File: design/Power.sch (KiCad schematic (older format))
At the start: 50 parts, among them U2 NCP1117ST33T3G, U3 DRV8302

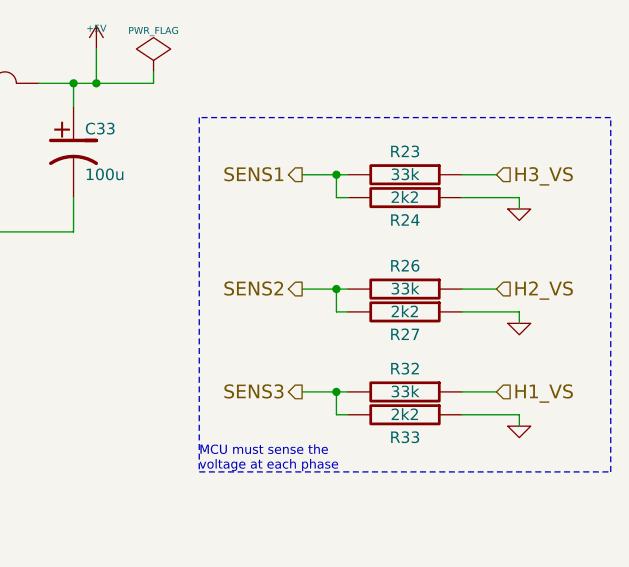
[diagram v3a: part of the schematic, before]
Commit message: Changed voltage divider resistor to 39k
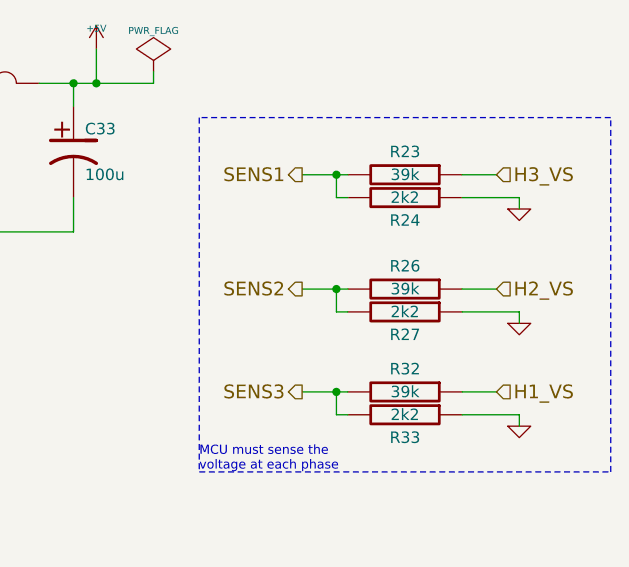
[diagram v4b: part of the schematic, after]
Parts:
- R23, R26, R32: value 33k -> 39k
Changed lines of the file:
@@
 LIBS:crf_1
 LIBS:BLDC_4-cache
-EELAYER 25 0
+EELAYER 24 0
 EELAYER END
 $Descr A4 11693 8268
@@
 P 10200 3350
 F 0 "R23" V 10100 3350 50  0000 C CNN
-F 1 "33k" V 10200 3350 50  0000 C CNN
+F 1 "39k" V 10200 3350 50  0000 C CNN
 F 2 "SMD_Packages:SMD-0603_r" H 10200 3350 60  0001 C CNN
 F 3 "" H 10200 3350 60  0001 C CNN
@@
 P 10200 3850
 F 0 "R26" V 10100 3850 50  0000 C CNN
-F 1 "33k" V 10200 3850 50  0000 C CNN
+F 1 "39k" V 10200 3850 50  0000 C CNN
 F 2 "SMD_Packages:SMD-0603_r" H 10200 3850 60  0001 C CNN
 F 3 "" H 10200 3850 60  0001 C CNN
@@
 P 10200 4300
 F 0 "R32" V 10100 4300 50  0000 C CNN
-F 1 "33k" V 10200 4300 50  0000 C CNN
+F 1 "39k" V 10200 4300 50  0000 C CNN
 F 2 "SMD_Packages:SMD-0603_r" H 10200 4300 60  0001 C CNN
 F 3 "" H 10200 4300 60  0001 C CNN
@@
 00 FD 87 A8 17 00 00 00 00 F4 1F A2 5E 00 00 00 00 D0 7F 88 7A 01 00 00 00 40 FF 21 EA 05 00 00
 00 00 FD 87 A8 17 00 00 00 00 F4 1F A2 5E 00 00 00 00 D0 7F 88 7A 01 00 00 00 40 FF 21 EA 05 00
-00 00 00 FD F7 3F 90 37 91 24 49 74 FD E2 00 00 00 00 49 45 4E 44 AE 42 60 82 00
+00 00 00 FD F7 3F 90 37 91 24 49 74 FD E2 00 00 00 00 49 45 4E 44 AE 42 60 82 2E
 EndData
 $EndBitmap
@@
 0D 0D 85 50 5B 08 A1 71 E3 C6 45 47 47 77 AB F8 CD C0 F0 65 C3 18 9A 0F 4F 4B 4B 4B 51 51 51 53
 53 93 40 20 30 31 31 61 94 40 19 18 18 43 C3 C0 C0 A0 72 FE 07 CF 64 8C 61 E1 12 74 DD 00 00 00
-00 49 45 4E 44 AE 42 60 82 05
+00 49 45 4E 44 AE 42 60 82 6A
 EndData
 $EndBitmap
@@
 20 10 88 31 C3 77 F3 62 81 40 20 10 08 04 02 81 E0 1F 14 E4 21 10 08 04 02 81 40 8C 41 50 90 87
 40 20 10 08 04 02 31 06 41 41 1E 02 81 40 20 10 08 C4 18 E4 FF 01 14 B1 03 90 4A B9 68 69 00 00
-00 00 49 45 4E 44 AE 42 60 82 00
+00 00 49 45 4E 44 AE 42 60 82 2D
 EndData
 $EndBitmap
@@
 A1 C7 18 00 00 C0 28 C8 B2 00 00 00 46 41 96 05 00 00 30 0A B2 2C 00 00 80 51 90 65 01 00 00 8C
 82 2C 0B 00 00 60 14 64 59 00 00 00 A3 FC 7F BD 9B 69 A6 C1 67 F0 EA 00 00 00 00 49 45 4E 44 AE
-42 60 82 00
+42 60 82 6B
 EndData
 $EndBitmap
@@
 AB D8 39 0B 59 91 9E DF A8 2A 5B EE 54 3A FD 71 ED 71 2F 29 C3 82 EC 80 87 06 6E C3 98 10 30 3B
 62 9A BB 2D 03 B8 C4 64 FC B5 26 AC 13 9B D1 39 40 41 C1 D6 78 4C 84 BF 94 F0 6F E1 BF 96 F0 0F
-FF 77 E2 FF 1F 0F 43 55 32 21 1C 08 16 00 00 00 00 49 45 4E 44 AE 42 60 82 27
+FF 77 E2 FF 1F 0F 43 55 32 21 1C 08 16 00 00 00 00 49 45 4E 44 AE 42 60 82 60
 EndData
 $EndBitmap

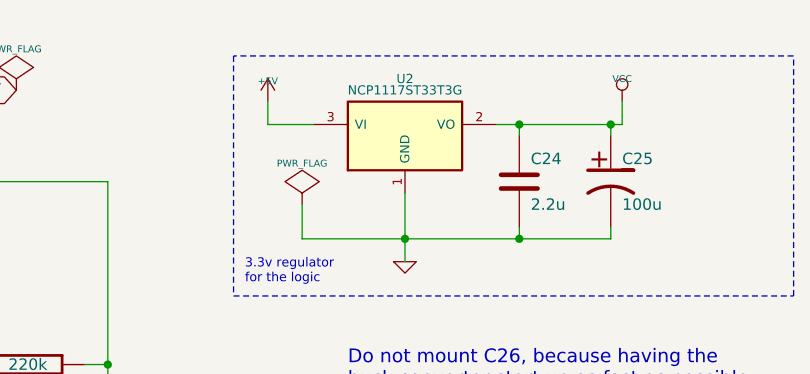
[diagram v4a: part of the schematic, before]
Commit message: Changed FETs and VREG part number to make things a bit more clear
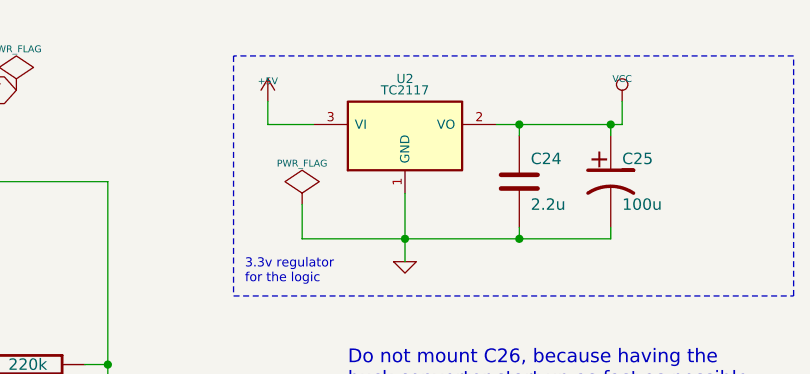
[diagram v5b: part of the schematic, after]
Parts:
- U2: value NCP1117ST33T3G -> TC2117
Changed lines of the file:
@@
 P 6300 1200
 F 0 "U2" H 6300 1450 40  0000 C CNN
-F 1 "NCP1117ST33T3G" H 6300 1400 40  0000 C CNN
+F 1 "TC2117" H 6300 1400 40  0000 C CNN
 F 2 "SMD_Packages:SOT-223" H 6300 1200 60  0001 C CNN
 F 3 "" H 6300 1200 60  0000 C CNN
@@
 00 FD 87 A8 17 00 00 00 00 F4 1F A2 5E 00 00 00 00 D0 7F 88 7A 01 00 00 00 40 FF 21 EA 05 00 00
 00 00 FD 87 A8 17 00 00 00 00 F4 1F A2 5E 00 00 00 00 D0 7F 88 7A 01 00 00 00 40 FF 21 EA 05 00
-00 00 00 FD F7 3F 90 37 91 24 49 74 FD E2 00 00 00 00 49 45 4E 44 AE 42 60 82 2E
+00 00 00 FD F7 3F 90 37 91 24 49 74 FD E2 00 00 00 00 49 45 4E 44 AE 42 60 82 4D
 EndData
 $EndBitmap
@@
 0D 0D 85 50 5B 08 A1 71 E3 C6 45 47 47 77 AB F8 CD C0 F0 65 C3 18 9A 0F 4F 4B 4B 4B 51 51 51 53
 53 93 40 20 30 31 31 61 94 40 19 18 18 43 C3 C0 C0 A0 72 FE 07 CF 64 8C 61 E1 12 74 DD 00 00 00
-00 49 45 4E 44 AE 42 60 82 6A
+00 49 45 4E 44 AE 42 60 82 32
 EndData
 $EndBitmap
@@
 20 10 88 31 C3 77 F3 62 81 40 20 10 08 04 02 81 E0 1F 14 E4 21 10 08 04 02 81 40 8C 41 50 90 87
 40 20 10 08 04 02 31 06 41 41 1E 02 81 40 20 10 08 C4 18 E4 FF 01 14 B1 03 90 4A B9 68 69 00 00
-00 00 49 45 4E 44 AE 42 60 82 2D
+00 00 49 45 4E 44 AE 42 60 82 4C
 EndData
 $EndBitmap
@@
 A1 C7 18 00 00 C0 28 C8 B2 00 00 00 46 41 96 05 00 00 30 0A B2 2C 00 00 80 51 90 65 01 00 00 8C
 82 2C 0B 00 00 60 14 64 59 00 00 00 A3 FC 7F BD 9B 69 A6 C1 67 F0 EA 00 00 00 00 49 45 4E 44 AE
-42 60 82 6B
+42 60 82 D7
 EndData
 $EndBitmap
@@
 AB D8 39 0B 59 91 9E DF A8 2A 5B EE 54 3A FD 71 ED 71 2F 29 C3 82 EC 80 87 06 6E C3 98 10 30 3B
 62 9A BB 2D 03 B8 C4 64 FC B5 26 AC 13 9B D1 39 40 41 C1 D6 78 4C 84 BF 94 F0 6F E1 BF 96 F0 0F
-FF 77 E2 FF 1F 0F 43 55 32 21 1C 08 16 00 00 00 00 49 45 4E 44 AE 42 60 82 60
+FF 77 E2 FF 1F 0F 43 55 32 21 1C 08 16 00 00 00 00 49 45 4E 44 AE 42 60 82 47
 EndData
 $EndBitmap

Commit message: HW4.8: better shunt routing, extra pin on comm connector, footprint fixed, zone fixes, many other improvements
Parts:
- removed C26: 15n, SMD_Packages:SMD-0603_c, symbol C
- removed R15: 330k, SMD_Packages:SMD-0603_r, symbol R
- removed R16: 10k, SMD_Packages:SMD-0603_r, symbol R
- C1, C39, C40, C43, C44, C49, C8, C9: footprint SMD_Packages:SMD-1206 -> CRF1:SMD-1206; symbol C -> C-RESCUE-BLDC_4
- C18, C23, C28, C29, C30: footprint SMD_Packages:SMD-0805 -> CRF1:SMD-0603_c; symbol C -> C-RESCUE-BLDC_4
- C19, C20, C21, C22, C24, C27, C34, C36, C52: footprint SMD_Packages:SMD-0603_c -> CRF1:SMD-0603_c; symbol C -> C-RESCUE-BLDC_4
- C25, C33: symbol CP1 -> CP1-RESCUE-BLDC_4
- C37, C51: symbol C -> C-RESCUE-BLDC_4
- D4: footprint Diodes_SMD:Diode-SMA_Handsoldering -> Diodes_SMD:SMA_Handsoldering
- R17, R18, R19, R20, R21, R23, R24, R25, R26, R27, R32, R33, R48, R49, R50, R51: footprint SMD_Packages:SMD-0603_r -> CRF1:SMD-0603_r; symbol R -> R-RESCUE-BLDC_4
- U2: footprint SMD_Packages:SOT-223 -> CRF1:SOT-223
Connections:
- net at U3.11 (OC_ADJ): now also C20.2, C52.2, U3.23 (DVDD)
- no-connect marks 3 -> 4
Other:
- note removed: "Do not mount C26, because having the\nbuck converter start up as fast as possible\nin case of a power dip is better."
- note removed: "Do not mount the resistor R16, because\nthe internal current limit in the DRV8302\ndoes not work with this configuration for\nsome reason. If this resistor is mounted, \nthe DRV8203 will generate faults all the time."
- moved on the sheet: C1, C37, C40, C51, C8, C9
